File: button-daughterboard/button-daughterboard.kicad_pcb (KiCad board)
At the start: 2 copper layers, 130.5 x 25 mm, 25 parts, among them J1 Conn_01x01, J2 Conn_01x01, J3 Conn_01x01, J4 Conn_01x01, J5 Conn_01x01, J6 Conn_01x01, J7 Conn_01x01, J8 Conn_01x01, SW1 SW_Push, SW2 SW_Push, SW3 SW_Push, SW4 SW_Push, SW5 SW_Push, SW6 SW_Push

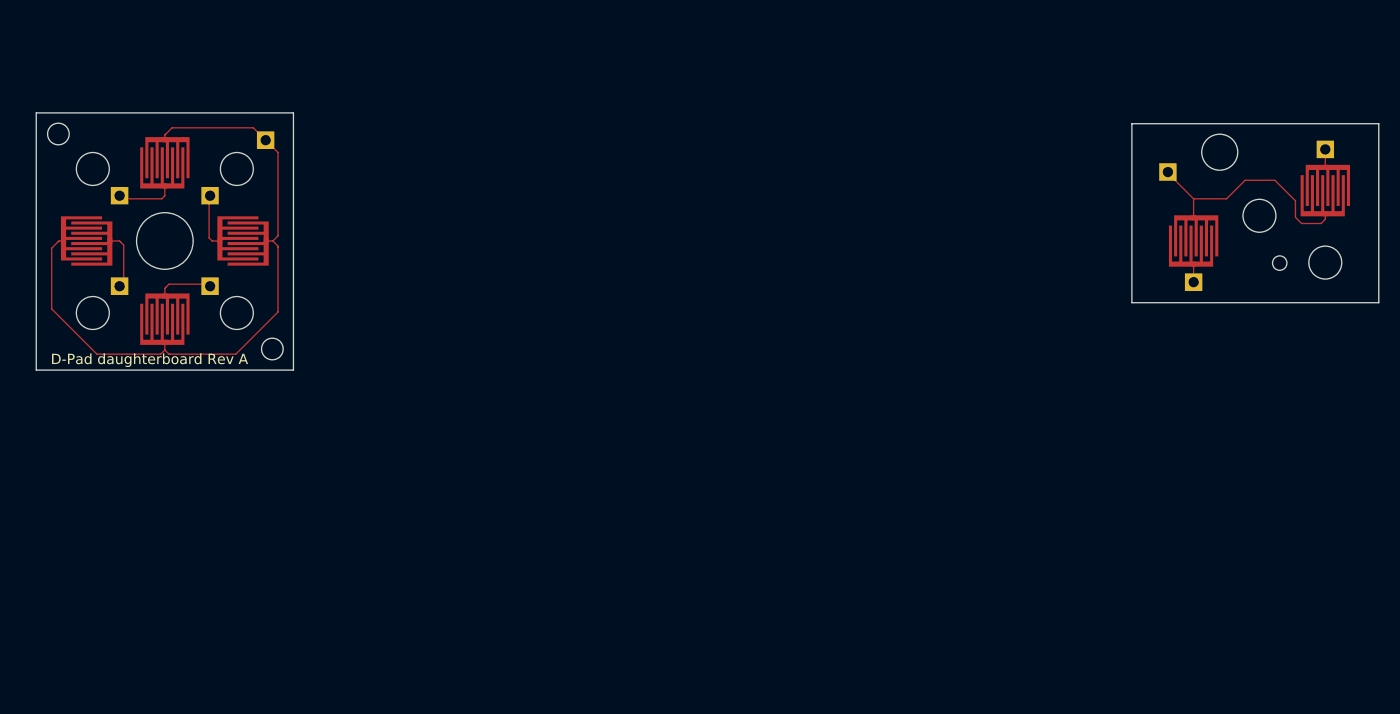
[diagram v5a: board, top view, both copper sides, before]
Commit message: Panelize button daughterboards
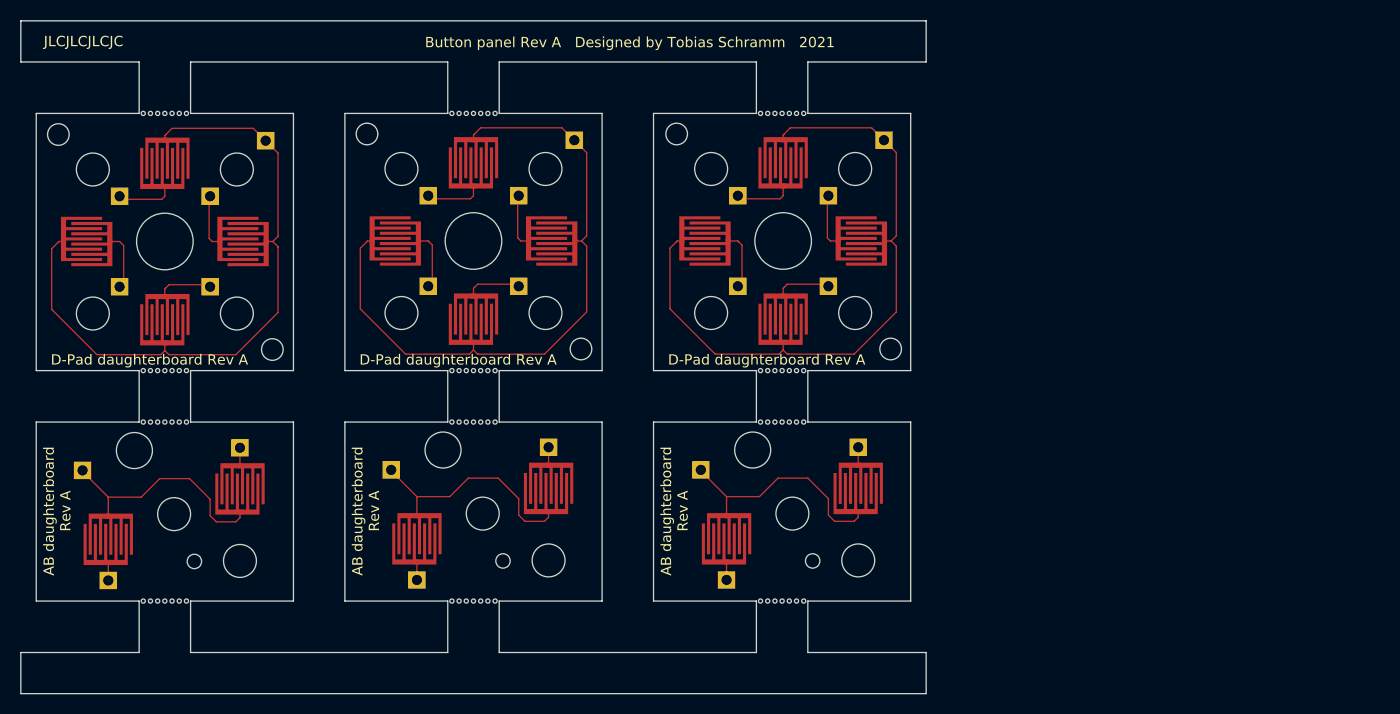
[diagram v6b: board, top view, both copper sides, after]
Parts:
- added H12: D-Pad Hole, MountingHole:MountingHole_5.5mm, F.Cu at (130.0, 100.0)
- added H13: D-Pad top left, MountingHole_GameBoy:MountingHole_GameBoy_DPAD, F.Cu at (119.7, 89.6)
- added H14: D-Pad bottom right, MountingHole_GameBoy:MountingHole_GameBoy_DPAD, F.Cu at (140.4, 110.5)
- added H15: MountingHole, MountingHole:MountingHole_3.2mm_M3, F.Cu at (123.0, 93.0)
- added H16: MountingHole, MountingHole:MountingHole_3.2mm_M3, F.Cu at (137.0, 107.0)
- added H17: MountingHole, MountingHole:MountingHole_3.2mm_M3, F.Cu at (137.0, 93.0)
- added H18: MountingHole, MountingHole:MountingHole_3.2mm_M3, F.Cu at (123.0, 107.0)
- added H19: AB top left, MountingHole:MountingHole_3.5mm, F.Cu at (127.0, 120.3)
- added H20: AB bottom right, MountingHole_GBA:MountingHole_GBA_AB_bottom_right, F.Cu at (132.9, 131.1)
- added H21: MountingHole, MountingHole:MountingHole_3.2mm_M3, F.Cu at (130.9, 126.5)
- added H22: MountingHole, MountingHole:MountingHole_3.2mm_M3, F.Cu at (137.3, 131.1)
- added H23: D-Pad Hole, MountingHole:MountingHole_5.5mm, F.Cu at (160.1, 100.0)
- added H24: D-Pad top left, MountingHole_GameBoy:MountingHole_GameBoy_DPAD, F.Cu at (149.8, 89.6)
- added H25: D-Pad bottom right, MountingHole_GameBoy:MountingHole_GameBoy_DPAD, F.Cu at (170.6, 110.5)
- added H26: MountingHole, MountingHole:MountingHole_3.2mm_M3, F.Cu at (153.1, 93.0)
- added H27: MountingHole, MountingHole:MountingHole_3.2mm_M3, F.Cu at (167.1, 107.0)
- added H28: MountingHole, MountingHole:MountingHole_3.2mm_M3, F.Cu at (167.1, 93.0)
- added H29: MountingHole, MountingHole:MountingHole_3.2mm_M3, F.Cu at (153.1, 107.0)
- added H30: AB top left, MountingHole:MountingHole_3.5mm, F.Cu at (157.1, 120.3)
- added H31: AB bottom right, MountingHole_GBA:MountingHole_GBA_AB_bottom_right, F.Cu at (163.0, 131.1)
- added H32: MountingHole, MountingHole:MountingHole_3.2mm_M3, F.Cu at (161.0, 126.5)
- added H33: MountingHole, MountingHole:MountingHole_3.2mm_M3, F.Cu at (167.4, 131.1)
- added J10: Conn_01x01, Connector_PinHeader_2.54mm:PinHeader_1x01_P2.54mm_Vertical, B.Cu at (125.6, 104.4)
- added J11: Conn_01x01, Connector_PinHeader_2.54mm:PinHeader_1x01_P2.54mm_Vertical, B.Cu at (134.4, 104.4)
- added J12: Conn_01x01, Connector_PinHeader_2.54mm:PinHeader_1x01_P2.54mm_Vertical, B.Cu at (125.6, 95.6)
- added J13: Conn_01x01, Connector_PinHeader_2.54mm:PinHeader_1x01_P2.54mm_Vertical, B.Cu at (139.8, 90.2)
- added J14: Conn_01x01, Connector_PinHeader_2.54mm:PinHeader_1x01_P2.54mm_Vertical, B.Cu at (124.5, 132.9)
- added J15: Conn_01x01, Connector_PinHeader_2.54mm:PinHeader_1x01_P2.54mm_Vertical, B.Cu at (137.3, 120.0)
- added J16: Conn_01x01, Connector_PinHeader_2.54mm:PinHeader_1x01_P2.54mm_Vertical, B.Cu at (122.0, 122.2)
- added J17: Conn_01x01, Connector_PinHeader_2.54mm:PinHeader_1x01_P2.54mm_Vertical, B.Cu at (164.5, 95.6)
- added J18: Conn_01x01, Connector_PinHeader_2.54mm:PinHeader_1x01_P2.54mm_Vertical, B.Cu at (155.7, 104.4)
- added J19: Conn_01x01, Connector_PinHeader_2.54mm:PinHeader_1x01_P2.54mm_Vertical, B.Cu at (164.5, 104.4)
- added J20: Conn_01x01, Connector_PinHeader_2.54mm:PinHeader_1x01_P2.54mm_Vertical, B.Cu at (155.7, 95.6)
- added J21: Conn_01x01, Connector_PinHeader_2.54mm:PinHeader_1x01_P2.54mm_Vertical, B.Cu at (169.9, 90.2)
- added J22: Conn_01x01, Connector_PinHeader_2.54mm:PinHeader_1x01_P2.54mm_Vertical, B.Cu at (154.6, 132.9)
- added J23: Conn_01x01, Connector_PinHeader_2.54mm:PinHeader_1x01_P2.54mm_Vertical, B.Cu at (167.4, 120.0)
- added J24: Conn_01x01, Connector_PinHeader_2.54mm:PinHeader_1x01_P2.54mm_Vertical, B.Cu at (152.1, 122.2)
- added J9: Conn_01x01, Connector_PinHeader_2.54mm:PinHeader_1x01_P2.54mm_Vertical, B.Cu at (134.4, 95.6)
- added REF**: Perforation_0.4mm, Perforation:Perforation_0.4mm, F.Cu at (160.0, 117.6)
- added REF**: Perforation_0.4mm, Perforation:Perforation_0.4mm, F.Cu at (130.7, 117.6)
- added REF**: Perforation_0.4mm, Perforation:Perforation_0.4mm, F.Cu at (158.6, 117.6)
- added REF**: Perforation_0.4mm, Perforation:Perforation_0.4mm, F.Cu at (128.6, 117.6)
- added REF**: Perforation_0.4mm, Perforation:Perforation_0.4mm, F.Cu at (157.9, 117.6)
- added REF**: Perforation_0.4mm, Perforation:Perforation_0.4mm, F.Cu at (127.9, 117.6)
- added REF**: Perforation_0.4mm, Perforation:Perforation_0.4mm, F.Cu at (97.9, 117.6)
- added REF**: Perforation_0.4mm, Perforation:Perforation_0.4mm, F.Cu at (98.6, 117.6)
- added REF**: Perforation_0.4mm, Perforation:Perforation_0.4mm, F.Cu at (100.7, 117.6)
- added REF**: Perforation_0.4mm, Perforation:Perforation_0.4mm, F.Cu at (102.1, 117.6)
- added REF**: Perforation_0.4mm, Perforation:Perforation_0.4mm, F.Cu at (99.3, 117.6)
- added REF**: Perforation_0.4mm, Perforation:Perforation_0.4mm, F.Cu at (130.0, 117.6)
- added REF**: Perforation_0.4mm, Perforation:Perforation_0.4mm, F.Cu at (100.0, 117.6)
- added REF**: Perforation_0.4mm, Perforation:Perforation_0.4mm, F.Cu at (101.4, 117.6)
- added REF**: Perforation_0.4mm, Perforation:Perforation_0.4mm, F.Cu at (161.4, 135.0)
- added REF**: Perforation_0.4mm, Perforation:Perforation_0.4mm, F.Cu at (131.4, 135.0)
- added REF**: Perforation_0.4mm, Perforation:Perforation_0.4mm, F.Cu at (160.7, 135.0)
- added REF**: Perforation_0.4mm, Perforation:Perforation_0.4mm, F.Cu at (130.7, 135.0)
- added REF**: Perforation_0.4mm, Perforation:Perforation_0.4mm, F.Cu at (157.9, 135.0)
- added REF**: Perforation_0.4mm, Perforation:Perforation_0.4mm, F.Cu at (127.9, 135.0)
- added REF**: Perforation_0.4mm, Perforation:Perforation_0.4mm, F.Cu at (159.3, 135.0)
- added REF**: Perforation_0.4mm, Perforation:Perforation_0.4mm, F.Cu at (129.3, 135.0)
- added REF**: Perforation_0.4mm, Perforation:Perforation_0.4mm, F.Cu at (161.4, 117.6)
- added REF**: Perforation_0.4mm, Perforation:Perforation_0.4mm, F.Cu at (162.1, 135.0)
- added REF**: Perforation_0.4mm, Perforation:Perforation_0.4mm, F.Cu at (132.1, 135.0)
- added REF**: Perforation_0.4mm, Perforation:Perforation_0.4mm, F.Cu at (158.6, 135.0)
- added REF**: Perforation_0.4mm, Perforation:Perforation_0.4mm, F.Cu at (128.6, 135.0)
- added REF**: Perforation_0.4mm, Perforation:Perforation_0.4mm, F.Cu at (160.0, 135.0)
- added REF**: Perforation_0.4mm, Perforation:Perforation_0.4mm, F.Cu at (130.0, 135.0)
- added REF**: Perforation_0.4mm, Perforation:Perforation_0.4mm, F.Cu at (97.9, 135.0)
- added REF**: Perforation_0.4mm, Perforation:Perforation_0.4mm, F.Cu at (98.6, 135.0)
- added REF**: Perforation_0.4mm, Perforation:Perforation_0.4mm, F.Cu at (100.7, 135.0)
- added REF**: Perforation_0.4mm, Perforation:Perforation_0.4mm, F.Cu at (102.1, 135.0)
- added REF**: Perforation_0.4mm, Perforation:Perforation_0.4mm, F.Cu at (131.4, 117.6)
- added REF**: Perforation_0.4mm, Perforation:Perforation_0.4mm, F.Cu at (99.3, 135.0)
- added REF**: Perforation_0.4mm, Perforation:Perforation_0.4mm, F.Cu at (100.0, 135.0)
- added REF**: Perforation_0.4mm, Perforation:Perforation_0.4mm, F.Cu at (101.4, 135.0)
- added REF**: Perforation_0.4mm, Perforation:Perforation_0.4mm, F.Cu at (158.6, 112.6)
- added REF**: Perforation_0.4mm, Perforation:Perforation_0.4mm, F.Cu at (128.6, 112.6)
- added REF**: Perforation_0.4mm, Perforation:Perforation_0.4mm, F.Cu at (160.7, 112.6)
- added REF**: Perforation_0.4mm, Perforation:Perforation_0.4mm, F.Cu at (130.7, 112.6)
- added REF**: Perforation_0.4mm, Perforation:Perforation_0.4mm, F.Cu at (161.4, 112.6)
- added REF**: Perforation_0.4mm, Perforation:Perforation_0.4mm, F.Cu at (131.4, 112.6)
- added REF**: Perforation_0.4mm, Perforation:Perforation_0.4mm, F.Cu at (160.0, 112.6)
- added REF**: Perforation_0.4mm, Perforation:Perforation_0.4mm, F.Cu at (159.3, 117.6)
- added REF**: Perforation_0.4mm, Perforation:Perforation_0.4mm, F.Cu at (130.0, 112.6)
- added REF**: Perforation_0.4mm, Perforation:Perforation_0.4mm, F.Cu at (162.1, 112.6)
- added REF**: Perforation_0.4mm, Perforation:Perforation_0.4mm, F.Cu at (132.1, 112.6)
- added REF**: Perforation_0.4mm, Perforation:Perforation_0.4mm, F.Cu at (159.3, 112.6)
- added REF**: Perforation_0.4mm, Perforation:Perforation_0.4mm, F.Cu at (129.3, 112.6)
- added REF**: Perforation_0.4mm, Perforation:Perforation_0.4mm, F.Cu at (157.9, 112.6)
- added REF**: Perforation_0.4mm, Perforation:Perforation_0.4mm, F.Cu at (127.9, 112.6)
- added REF**: Perforation_0.4mm, Perforation:Perforation_0.4mm, F.Cu at (97.9, 112.6)
- added REF**: Perforation_0.4mm, Perforation:Perforation_0.4mm, F.Cu at (98.6, 112.6)
- added REF**: Perforation_0.4mm, Perforation:Perforation_0.4mm, F.Cu at (100.7, 112.6)
- added REF**: Perforation_0.4mm, Perforation:Perforation_0.4mm, F.Cu at (129.3, 117.6)
- added REF**: Perforation_0.4mm, Perforation:Perforation_0.4mm, F.Cu at (102.1, 112.6)
- added REF**: Perforation_0.4mm, Perforation:Perforation_0.4mm, F.Cu at (99.3, 112.6)
- added REF**: Perforation_0.4mm, Perforation:Perforation_0.4mm, F.Cu at (100.0, 112.6)
- added REF**: Perforation_0.4mm, Perforation:Perforation_0.4mm, F.Cu at (101.4, 112.6)
- added REF**: Perforation_0.4mm, Perforation:Perforation_0.4mm, F.Cu at (157.9, 87.6)
- added REF**: Perforation_0.4mm, Perforation:Perforation_0.4mm, F.Cu at (127.9, 87.6)
- added REF**: Perforation_0.4mm, Perforation:Perforation_0.4mm, F.Cu at (158.6, 87.6)
- added REF**: Perforation_0.4mm, Perforation:Perforation_0.4mm, F.Cu at (128.6, 87.6)
- added REF**: Perforation_0.4mm, Perforation:Perforation_0.4mm, F.Cu at (160.7, 87.6)
- added REF**: Perforation_0.4mm, Perforation:Perforation_0.4mm, F.Cu at (130.7, 87.6)
- added REF**: Perforation_0.4mm, Perforation:Perforation_0.4mm, F.Cu at (162.1, 117.6)
- added REF**: Perforation_0.4mm, Perforation:Perforation_0.4mm, F.Cu at (162.1, 87.6)
- added REF**: Perforation_0.4mm, Perforation:Perforation_0.4mm, F.Cu at (132.1, 87.6)
- added REF**: Perforation_0.4mm, Perforation:Perforation_0.4mm, F.Cu at (159.3, 87.6)
- added REF**: Perforation_0.4mm, Perforation:Perforation_0.4mm, F.Cu at (129.3, 87.6)
- added REF**: Perforation_0.4mm, Perforation:Perforation_0.4mm, F.Cu at (160.0, 87.6)
- added REF**: Perforation_0.4mm, Perforation:Perforation_0.4mm, F.Cu at (130.0, 87.6)
- added REF**: Perforation_0.4mm, Perforation:Perforation_0.4mm, F.Cu at (161.4, 87.6)
- added REF**: Perforation_0.4mm, Perforation:Perforation_0.4mm, F.Cu at (131.4, 87.6)
- added REF**: Perforation_0.4mm, Perforation:Perforation_0.4mm, F.Cu at (102.1, 87.6)
- added REF**: Perforation_0.4mm, Perforation:Perforation_0.4mm, F.Cu at (101.4, 87.6)
- added REF**: Perforation_0.4mm, Perforation:Perforation_0.4mm, F.Cu at (132.1, 117.6)
- added REF**: Perforation_0.4mm, Perforation:Perforation_0.4mm, F.Cu at (100.7, 87.6)
- added REF**: Perforation_0.4mm, Perforation:Perforation_0.4mm, F.Cu at (100.0, 87.6)
- added REF**: Perforation_0.4mm, Perforation:Perforation_0.4mm, F.Cu at (99.3, 87.6)
- added REF**: Perforation_0.4mm, Perforation:Perforation_0.4mm, F.Cu at (98.6, 87.6)
- added REF**: Perforation_0.4mm, Perforation:Perforation_0.4mm, F.Cu at (97.9, 87.6)
- added REF**: Perforation_0.4mm, Perforation:Perforation_0.4mm, F.Cu at (160.7, 117.6)
- added SW10: SW_Push, Button_Carbon:Button_Carbon_5mm, F.Cu at (130.0, 92.4)
- added SW11: SW_Push, Button_Carbon:Button_Carbon_5mm, F.Cu at (124.5, 128.9)
- added SW12: SW_Push, Button_Carbon:Button_Carbon_5mm, F.Cu at (137.3, 124.0)
- added SW13: SW_Push, Button_Carbon:Button_Carbon_5mm, F.Cu at (167.7, 100.0)
- added SW14: SW_Push, Button_Carbon:Button_Carbon_5mm, F.Cu at (152.5, 100.0)
- added SW15: SW_Push, Button_Carbon:Button_Carbon_5mm, F.Cu at (160.1, 107.6)
- added SW16: SW_Push, Button_Carbon:Button_Carbon_5mm, F.Cu at (160.1, 92.4)
- added SW17: SW_Push, Button_Carbon:Button_Carbon_5mm, F.Cu at (154.6, 128.9)
- added SW18: SW_Push, Button_Carbon:Button_Carbon_5mm, F.Cu at (167.4, 124.0)
- added SW7: SW_Push, Button_Carbon:Button_Carbon_5mm, F.Cu at (137.6, 100.0)
- added SW8: SW_Push, Button_Carbon:Button_Carbon_5mm, F.Cu at (122.4, 100.0)
- added SW9: SW_Push, Button_Carbon:Button_Carbon_5mm, F.Cu at (130.0, 107.6)
- moved H11 109.4 mm to (107.3, 131.1)
- moved J8 109.4 mm to (107.3, 120.1)
- moved SW6 109.4 mm to (107.3, 124.1)
- moved H10 109.4 mm to (100.9, 126.5)
- moved H9 109.4 mm to (102.9, 131.2)
- moved J6 109.4 mm to (94.5, 133.0)
- moved J7 109.4 mm to (92.0, 122.3)
- moved SW5 109.4 mm to (94.5, 129.0)
- moved H8 109.4 mm to (97.0, 120.4)
- moved H2 0.05 mm to (89.7, 89.7)
- moved J1 0.05 mm to (104.4, 95.7)
- moved J4 0.05 mm to (95.6, 95.7)
- moved SW3 0.05 mm to (100.0, 107.7)
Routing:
- net GND: track 85.9 -> 257.7 mm
- net Net-(J10-Pad1): track 0.00 -> 6.16 mm
- net Net-(J18-Pad1): track 0.00 -> 6.16 mm
- net Net-(J19-Pad1): track 0.00 -> 6.01 mm
- net Net-(J11-Pad1): track 0.00 -> 6.01 mm
- net Net-(J12-Pad1): track 0.00 -> 5.88 mm
- net Net-(J20-Pad1): track 0.00 -> 5.88 mm
- net Net-(J9-Pad1): track 0.00 -> 5.77 mm
- net Net-(J17-Pad1): track 0.00 -> 5.77 mm
- net Net-(J22-Pad1): track 0.00 -> 1.80 mm
- net Net-(J14-Pad1): track 0.00 -> 1.80 mm
- net Net-(J23-Pad1): track 0.00 -> 1.70 mm
- net Net-(J15-Pad1): track 0.00 -> 1.70 mm
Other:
- board size 130.5 x 25 mm -> 88 x 65.4 mm
- board text added: "AB daughterboard Rev A"
- board text added: "Button panel Rev A Designed by Tobias Schramm 2021"
- board text added: "JLCJLCJLCJC"
